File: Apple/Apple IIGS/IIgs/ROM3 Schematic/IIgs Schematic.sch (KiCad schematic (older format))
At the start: 0 parts

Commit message: More label style changes
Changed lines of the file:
@@
 encoding utf-8
 Sheet 1 10
-Title ""
+Title "Apple IIgs ROM3"
 Date ""
 Rev "2"
@@
 $EndDescr
 $Sheet
-S 1200 1150 1700 950
+S 1200 1150 1450 2700
 U 5BF1CF7D
 F0 "CYA-Mem-1" 50
 F1 "CYA-Mem-1.sch" 50
+F2 "IRQ.L" I R 2650 1250 50
+F3 "RESET.L" I R 2650 1350 50
+F4 "RDY.H" I R 2650 1450 50
+F5 "NMI.L" I R 2650 1550 50
+F6 "PH2.H" I R 2650 1650 50
+F7 "STRETCH.L" I R 2650 1750 50
+F8 "ABDIR.L" I R 2650 1850 50
+F9 "ABENB.L" I R 2650 1950 50
+F10 "DBENB.L" I R 2650 2050 50
+F11 "DBDIR.L" I R 2650 2200 50
+F12 "DMA.L" I L 1200 1900 50
+F13 "A2R-W.H" I L 1200 1800 50
+F14 "ROMSEL0.L" I L 1200 1700 50
+F15 "ROMOE-A16D" I L 1200 1600 50
+F16 "ROMSEL1.L" I L 1200 1500 50
+F17 "14MD.H" I L 1200 1400 50
+F18 "CASD" I L 1200 1300 50
+F19 "RASD" I L 1200 1200 50
+F20 "M2BA0" I R 2650 2400 50
+F21 "fastRR-W.H" I R 2650 2500 50
 $EndSheet
 $Sheet
@@
 F0 "Sound-8" 50
 F1 "Sound-8.sch" 50
+F2 "C038-F.L" I L 6700 5000 50
+F3 "7M.H" I L 6700 5150 50
+F4 "RESET.L" I L 6700 5250 50
+F5 "A2R-W.H" I L 6700 5350 50
+F6 "MDBUS[7..0]" I L 6700 5450 50
+F7 "BABUS1" I L 6700 5550 50
+F8 "BABUS0" I L 6700 5650 50
+F9 "IRQ.L" I L 6700 4900 50
+F10 "SOUND.H" I R 8150 5000 50
+F11 "SPKR.H" I R 8150 5100 50
 $EndSheet
 $Sheet

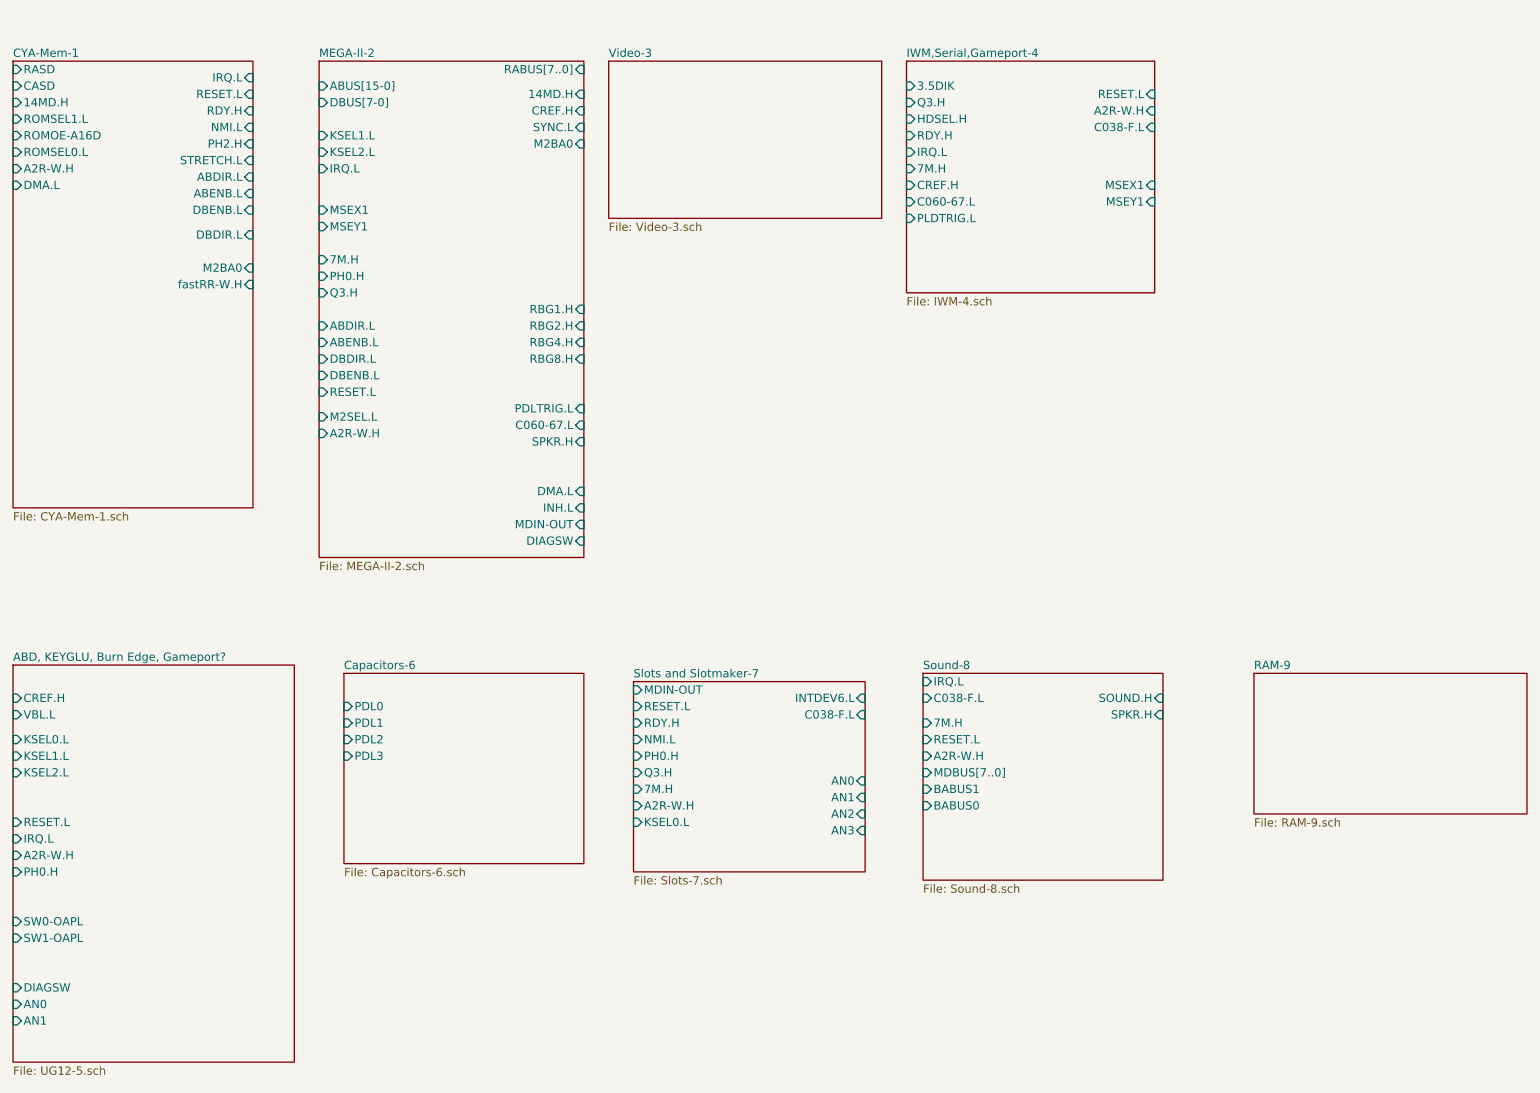
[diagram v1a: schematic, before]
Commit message: More hierarchical symbols added. changed symbol colors on CPU page
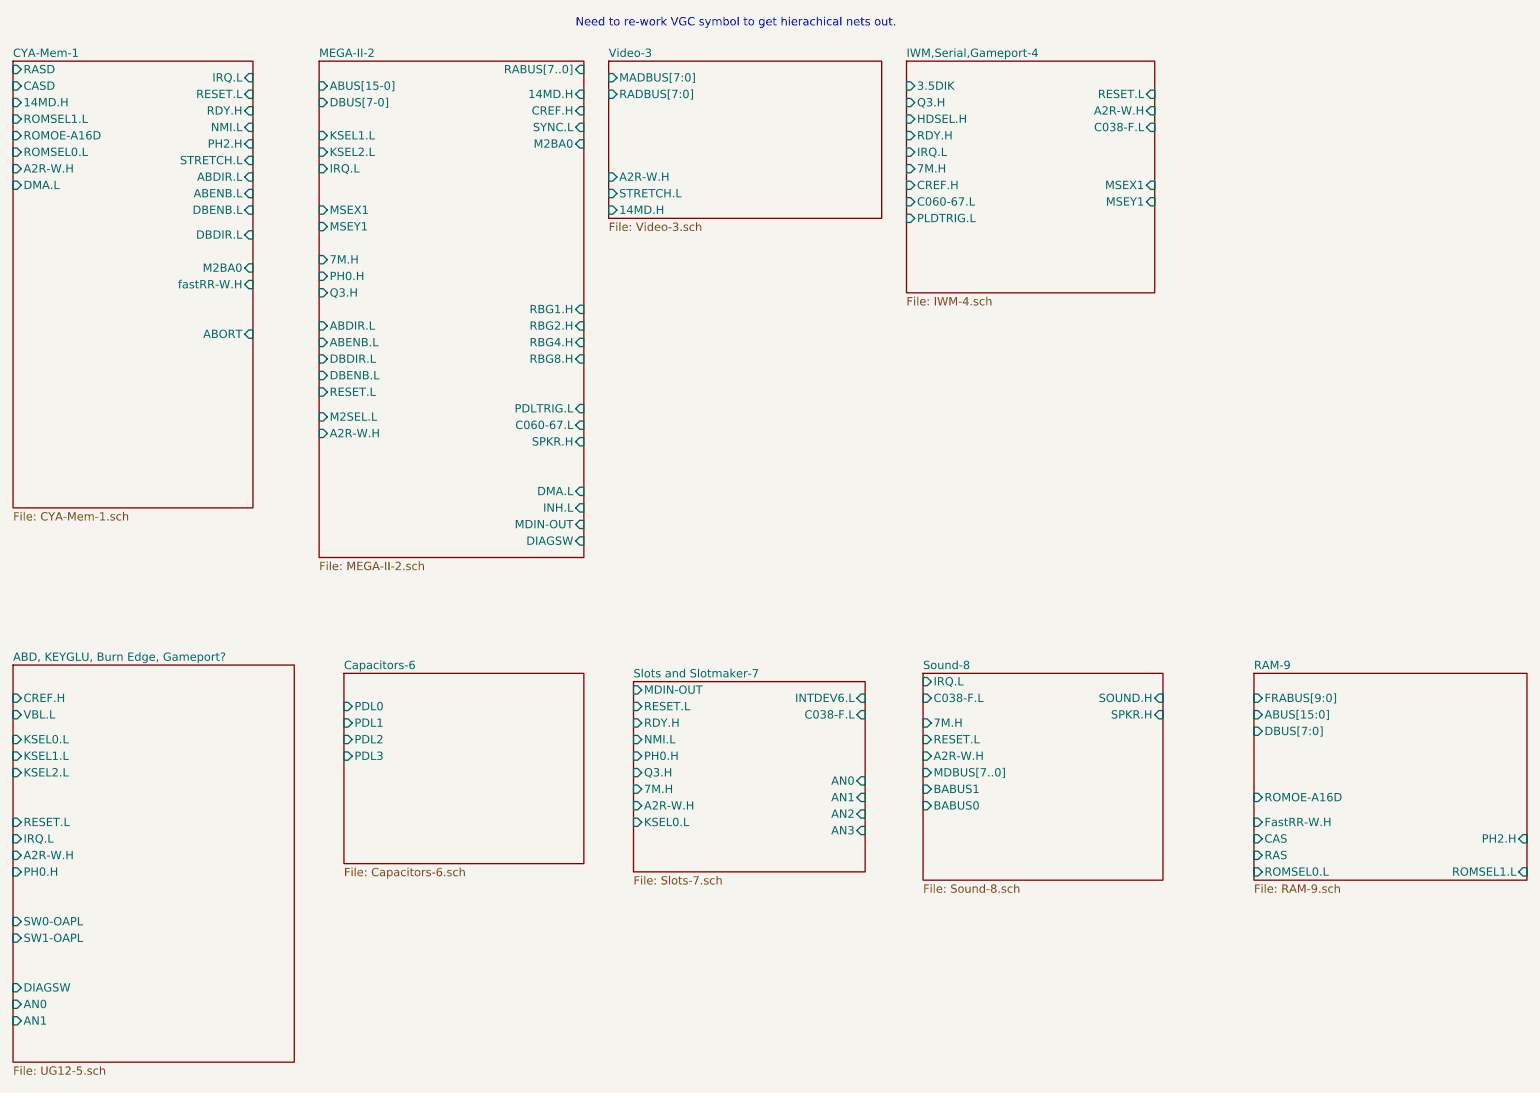
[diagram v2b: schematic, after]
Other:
- note added: "Need to re-work VGC symbol to get hierachical nets out."
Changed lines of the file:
@@
 F20 "M2BA0" I R 2650 2400 50
 F21 "fastRR-W.H" I R 2650 2500 50
+F22 "ABORT" I R 2650 2800 50
 $EndSheet
 $Sheet
@@
 F0 "Video-3" 50
 F1 "Video-3.sch" 50
+F2 "MADBUS[7:0]" I L 4800 1250 50
+F3 "RADBUS[7:0]" I L 4800 1350 50
+F4 "14MD.H" I L 4800 2050 50
+F5 "STRETCH.L" I L 4800 1950 50
+F6 "A2R-W.H" I L 4800 1850 50
 $EndSheet
 $Sheet
@@
 $EndSheet
 $Sheet
-S 8700 4850 1650 850
+S 8700 4850 1650 1250
 U 5BF22CDE
 F0 "RAM-9" 50
 F1 "RAM-9.sch" 50
+F2 "FRABUS[9:0]" I L 8700 5000 50
+F3 "RAS" I L 8700 5950 50
+F4 "CAS" I L 8700 5850 50
+F5 "FastRR-W.H" I L 8700 5750 50
+F6 "DBUS[7:0]" I L 8700 5200 50
+F7 "ABUS[15:0]" I L 8700 5100 50
+F8 "ROMOE-A16D" I L 8700 5600 50
+F9 "ROMSEL0.L" I L 8700 6050 50
+F10 "ROMSEL1.L" I R 10350 6050 50
+F11 "PH2.H" I R 10350 5850 50
 $EndSheet
 $Sheet
@@
 F34 "RABUS[7..0]" I R 4650 1200 50
 $EndSheet
+Text Notes 4600 950  0    50   ~ 0
+Need to re-work VGC symbol to get hierachical nets out.
 $EndSCHEMATC
